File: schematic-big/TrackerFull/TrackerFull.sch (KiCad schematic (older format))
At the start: 60 parts, among them J1 Conn_01x05_Male, J2 MUC-20PFFR-JS7001, J3 Battery, J5 Conn_01x04_Male, J6 78727-0001, Q1 DMG2305UXQ, Q2 DMG2305UXQ, Q3 DMG2305UXQ, SW1 PTS647SK38SMTR2LFS, U1 TLV62585PDRLR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

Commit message: rf
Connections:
- net 2.5v: no longer C9.1, U5.2
- net GPS_POWER: now also C9.1, U5.2
- no-connect marks 38 -> 45
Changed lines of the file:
@@
 Connection ~ 9250 8450
 Wire Wire Line
-	9250 8450 9250 8350
-Wire Wire Line
 	8650 8450 8650 8600
 Wire Wire Line
 	9700 8450 9550 8450
-Text Label 9250 8350 0    50   ~ 0
-2.5v
 $Comp
 L Device:R R6
@@
 Wire Wire Line
 	2950 7500 2950 7750
-Text Label 14650 4950 0    50   ~ 0
-VSIM
 Text GLabel 2950 7650 0    50   Input ~ 0
 BAT_IN
@@
 Text Label 7100 8700 0    50   ~ 0
 ANT_OUT
+NoConn ~ 8150 6350
+NoConn ~ 8150 6450
+NoConn ~ 8150 6550
+NoConn ~ 8150 6650
+NoConn ~ 8150 5850
+NoConn ~ 8150 5550
+NoConn ~ 8150 5450
+Wire Wire Line
+	9150 8450 9250 8450
 $EndSCHEMATC

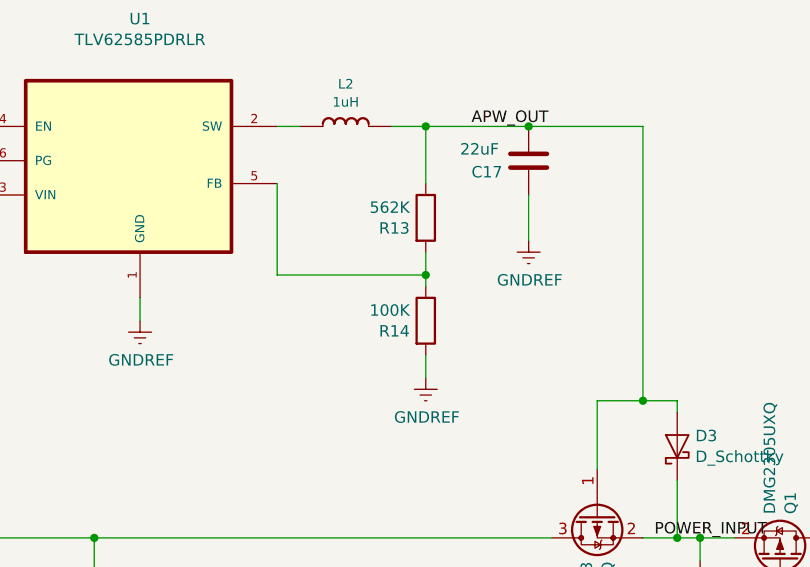
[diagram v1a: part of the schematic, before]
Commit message: attiny461 code update and new a9g footprint
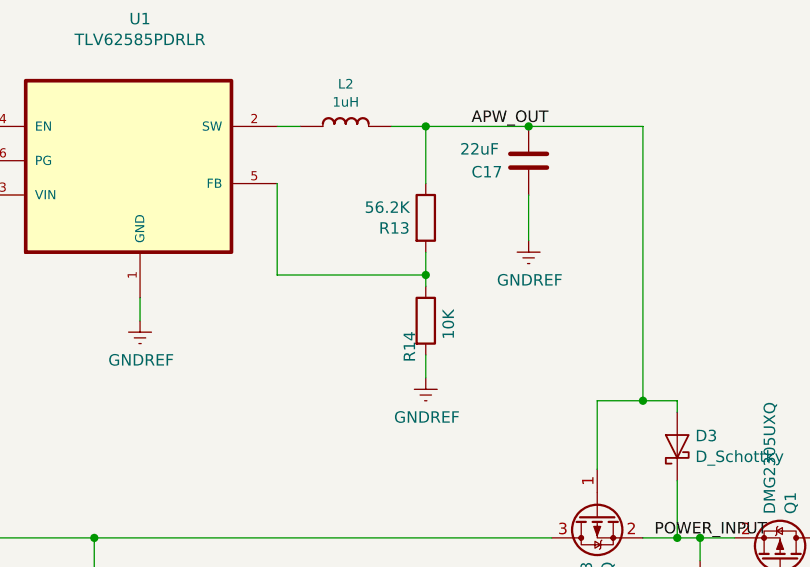
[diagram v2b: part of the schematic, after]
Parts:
- D1: footprint Tracker:A9G2 -> imported:A9
- R13: value 562K -> 56.2K; Поле5 CRCW0603562KFKEBC -> WR06X5622FTL
- R14: value 100K -> 10K; Поле5 CR161003F -> RMCF0603FG10K0
- R17, R5, R6, R7: footprint Resistor_SMD:R_0805_2012Metric_Pad1.15x1.40mm_HandSolder -> Resistor_SMD:R_0603_1608Metric; Поле5 CR0805-8W-103JT -> RMCF0603FG10K0
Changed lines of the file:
@@
 F 0 "R5" V 1830 3704 50  0000 R CNN
 F 1 "10K" V 2000 3800 50  0000 R CNN
-F 2 "Resistor_SMD:R_0805_2012Metric_Pad1.15x1.40mm_HandSolder" H 1830 3841 50  0001 R CNN
-F 3 "https://www.digikey.com/en/products/detail/venkel/CR0805-8W-103JT/12331089" H 1900 3750 50  0001 C CNN
-F 4 "CR0805-8W-103JT" H 1900 3750 50  0001 C CNN "Поле5"
+F 2 "Resistor_SMD:R_0603_1608Metric" H 1830 3841 50  0001 R CNN
+F 3 "https://www.digikey.com/en/products/detail/stackpole-electronics-inc/RMCF0603FG10K0/1761236" H 1900 3750 50  0001 C CNN
+F 4 "RMCF0603FG10K0" H 1900 3750 50  0001 C CNN "Поле5"
 	1    1900 3750
 	1    0    0    -1
@@
 F 0 "R17" V 3250 6350 50  0000 R CNN
 F 1 "10K" V 3200 6200 50  0000 R CNN
-F 2 "Resistor_SMD:R_0805_2012Metric_Pad1.15x1.40mm_HandSolder" H 3130 6241 50  0001 R CNN
-F 3 "https://www.digikey.com/en/products/detail/venkel/CR0805-8W-103JT/12331089" H 3200 6150 50  0001 C CNN
-F 4 "CR0805-8W-103JT" H 3200 6150 50  0001 C CNN "Поле5"
+F 2 "Resistor_SMD:R_0603_1608Metric" H 3130 6241 50  0001 R CNN
+F 3 "https://www.digikey.com/en/products/detail/stackpole-electronics-inc/RMCF0603FG10K0/1761236" H 3200 6150 50  0001 C CNN
+F 4 "RMCF0603FG10K0" H 3200 6150 50  0001 C CNN "Поле5"
 	1    3200 6150
 	0    -1   -1   0
@@
 F 0 "R7" V 3230 6504 50  0000 R CNN
 F 1 "10K" V 3150 6800 50  0000 R CNN
-F 2 "Resistor_SMD:R_0805_2012Metric_Pad1.15x1.40mm_HandSolder" H 3230 6641 50  0001 R CNN
-F 3 "https://www.digikey.com/en/products/detail/venkel/CR0805-8W-103JT/12331089" H 3300 6550 50  0001 C CNN
-F 4 "CR0805-8W-103JT" H 3300 6550 50  0001 C CNN "Поле5"
+F 2 "Resistor_SMD:R_0603_1608Metric" H 3230 6641 50  0001 R CNN
+F 3 "https://www.digikey.com/en/products/detail/stackpole-electronics-inc/RMCF0603FG10K0/1761236" H 3300 6550 50  0001 C CNN
+F 4 "RMCF0603FG10K0" H 3300 6550 50  0001 C CNN "Поле5"
 	1    3300 6550
 	0    -1   -1   0
@@
 F 0 "D1" H 4500 6106 50  0000 C CNN
 F 1 "A9G" H 4500 6015 50  0000 C CNN
-F 2 "Tracker:A9G2" V 3950 4450 50  0001 C CNN
+F 2 "imported:A9" V 3950 4450 50  0001 C CNN
 F 3 "https://www.alibaba.com/product-detail/GPRS-GPS-Module-A9G-Module-SMS_62458730712.html?spm=a2700.galleryofferlist.normal_offer.3.6881306fMlvXSR" V 3950 4450 50  0001 C CNN
 F 4 "3" H 4450 5500 50  0001 C CNN "Поле4"
@@
 F 0 "R6" V 8730 8404 50  0000 R CNN
 F 1 "10K" V 8900 8500 50  0000 R CNN
-F 2 "Resistor_SMD:R_0805_2012Metric_Pad1.15x1.40mm_HandSolder" H 8730 8541 50  0001 R CNN
-F 3 "https://www.digikey.com/en/products/detail/venkel/CR0805-8W-103JT/12331089" H 8800 8450 50  0001 C CNN
-F 4 "CR0805-8W-103JT" H 8800 8450 50  0001 C CNN "Поле5"
+F 2 "Resistor_SMD:R_0603_1608Metric" H 8730 8541 50  0001 R CNN
+F 3 "https://www.digikey.com/en/products/detail/stackpole-electronics-inc/RMCF0603FG10K0/1761236" H 8800 8450 50  0001 C CNN
+F 4 "RMCF0603FG10K0" H 8800 8450 50  0001 C CNN "Поле5"
 	1    8800 8450
 	0    -1   -1   0
@@
 P 8800 1450
 F 0 "R13" H 8730 1404 50  0000 R CNN
-F 1 "562K" H 8730 1495 50  0000 R CNN
+F 1 "56.2K" H 8730 1495 50  0000 R CNN
 F 2 "Resistor_SMD:R_0603_1608Metric" H 8730 1541 50  0001 R CNN
-F 3 "https://www.digikey.com/en/products/detail/vishay-dale/CRCW0603562KFKEBC/7925213" H 8800 1450 50  0001 C CNN
-F 4 "CRCW0603562KFKEBC" H 8800 1450 50  0001 C CNN "Поле5"
+F 3 "https://www.digikey.com/en/products/detail/walsin-technology-corporation/WR06X5622FTL/13241739" H 8800 1450 50  0001 C CNN
+F 4 "WR06X5622FTL" H 8800 1450 50  0001 C CNN "Поле5"
 	1    8800 1450
-	1    0    0    -1
-$EndComp
-$Comp
-L Device:R R14
-U 1 1 5FB5F89D
-P 8800 1900
-F 0 "R14" H 8730 1854 50  0000 R CNN
-F 1 "100K" H 8730 1945 50  0000 R CNN
-F 2 "Resistor_SMD:R_0603_1608Metric" H 8730 1991 50  0001 R CNN
-F 3 "https://www.digikey.com/en/products/detail/meritek/CR161003F/13412806" H 8800 1900 50  0001 C CNN
-F 4 "CR161003F" H 8800 1900 50  0001 C CNN "Поле5"
-	1    8800 1900
 	1    0    0    -1
 $EndComp
@@
 Wire Wire Line
 	9150 8450 9250 8450
+$Comp
+L Device:R R14
+U 1 1 5FB75EE7
+P 8800 1900
+F 0 "R14" V 8730 1854 50  0000 R CNN
+F 1 "10K" V 8900 1950 50  0000 R CNN
+F 2 "Resistor_SMD:R_0603_1608Metric" H 8730 1991 50  0001 R CNN
+F 3 "https://www.digikey.com/en/products/detail/stackpole-electronics-inc/RMCF0603FG10K0/1761236" H 8800 1900 50  0001 C CNN
+F 4 "RMCF0603FG10K0" H 8800 1900 50  0001 C CNN "Поле5"
+	1    8800 1900
+	1    0    0    -1
+$EndComp
 $EndSCHEMATC

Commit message: last changes
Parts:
- added C5: 100nF, Capacitor_SMD:C_0402_1005Metric, symbol Device:C
- added L1: 10uH, Inductor_SMD:L_0603_1608Metric, symbol Device:L
- added Q4: DMN60H080DS, Package_TO_SOT_SMD:SOT-23, symbol Device:Q_NMOS_GSD
- added R16, R20: 10K, Resistor_SMD:R_0603_1608Metric, symbol Device:R
- added R18: 470, Resistor_SMD:R_0402_1005Metric, symbol Device:R
- added R19: 5K, Resistor_SMD:R_0402_1005Metric, symbol Device:R
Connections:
- net 2.5v: now also U8.22 (AREF/PA3)
- net AVR_RST: now also R16.1
- net GNDD: now also C5.2, Q4.2 (S)
- net LOW_CURRENT: now also L1.1, R16.2, R19.1; no longer U8.18 (AVCC)
- net at U8.7 (XTAL1/PB4): now also R18.2
- net ADC_IN: now reaches U8.8 (XTAL2/PB5)
- net ADC_IN: now also R19.2, R20.2
- new net: Q4.3 (D), R20.1
- new net ADC_ENABLE: Q4.1 (G), R18.1
- new net AVCC: C5.1, L1.2, U8.18 (AVCC)
- no-connect marks 45 -> 42

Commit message: last changes
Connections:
- net ACCEL_INT1: now also U8.10 (PB6); no longer U8.25 (PA1)
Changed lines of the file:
@@
 Wire Wire Line
 	8800 1050 9250 1050
-Text Label 8300 5250 0    50   ~ 0
+Text Label 8300 6650 0    50   ~ 0
 ACCEL_INT1
 Wire Wire Line
@@
 	8150 5350 8300 5350
 Wire Wire Line
-	8150 5250 8300 5250
+	8150 6650 8300 6650
 Connection ~ 7450 4450
 Wire Wire Line
@@
 ANT_OUT
 NoConn ~ 8150 6350
-NoConn ~ 8150 6650
 NoConn ~ 8150 5850
 NoConn ~ 8150 5550
@@
 	1    0    0    -1
 $EndComp
+NoConn ~ 8150 5250
+Wire Notes Line
+	4050 450  4050 4350
+Wire Notes Line
+	4050 4350 450  4350
 $EndSCHEMATC

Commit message: last changes
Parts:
- removed SW1: PTS647SK38SMTR2LFS, PTS647SK38SMTR2LFS, symbol PTS647SK38SMTR2LFS:PTS647SK38SMTR2LFS
- R15: value 100K -> 10K; Поле5 CR161003F -> RMCF0603FG10K0
- U7: value MIC5232-2.8YD5 -> LDO-3v3; Поле5 MIC5232-2.8YD5 -> MIC5232-3.3YD5-TR
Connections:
- net 2.5v: now also C13.2, C18.2, L1.1, R16.2, U8.4 (VCC); no longer U8.22 (AREF/PA3)
- net GNDD: no longer J6.7 (DETECT_SPRING)
- net GNDREF: now also R15.2
- net LOW_CURRENT: now also J6.7 (DETECT_SPRING); no longer C13.2, C18.2, L1.1, R16.2, U8.4 (VCC)
- net POWER_INPUT: no longer R15.1
- net SIM_DETECT_LINE: now also R15.1; no longer R15.2
- no-connect marks 42 -> 43
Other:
- moved on the sheet: R16, R18, R3
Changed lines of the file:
@@
 BAT_IN
 NoConn ~ 4000 7500
-Connection ~ 8600 7350
-Wire Wire Line
-	8600 7350 8600 7450
-Wire Wire Line
-	9800 7350 9800 7450
-Connection ~ 9800 7450
-Wire Wire Line
-	9800 7450 9800 7600
 Wire Wire Line
 	3200 2050 3750 2050
@@
 Wire Wire Line
 	8800 1050 9250 1050
-Text Label 8300 6650 0    50   ~ 0
+Text Label 8400 6650 0    50   ~ 0
 ACCEL_INT1
 Wire Wire Line
@@
 Text Label 8600 6250 0    50   ~ 0
 ISP_SCK
-Wire Wire Line
-	8150 6750 8600 6750
 Text Label 8300 5150 0    50   ~ 0
 AVR_MOSI_SDA
@@
 	8150 5350 8300 5350
 Wire Wire Line
-	8150 6650 8300 6650
+	8150 6650 8400 6650
 Connection ~ 7450 4450
 Wire Wire Line
@@
 	7550 7050 7450 7050
 Connection ~ 7450 7050
-Text Label 9550 5650 0    50   ~ 0
+Text Label 9050 5650 0    50   ~ 0
 LED_CTL
 Text Label 9050 5750 0    50   ~ 0
@@
 	8900 5750 9050 5750
 Wire Wire Line
-	8150 5650 8800 5650
-Wire Wire Line
-	9100 5650 9550 5650
+	8150 5650 8600 5650
+Wire Wire Line
+	8900 5650 9050 5650
 Wire Wire Line
 	8150 5750 8600 5750
@@
 Wire Wire Line
 	650  1250 1350 1250
-Text Label 7450 4800 1    50   ~ 0
-LOW_CURRENT
 Text Label 11000 6000 0    50   ~ 0
 LOW_CURRENT
@@
 	1    0    0    -1
 $EndComp
-$Comp
-L power:GNDD #PWR0124
-U 1 1 602328E5
-P 9800 7600
-F 0 "#PWR0124" H 9800 7350 50  0001 C CNN
-F 1 "GNDD" H 9804 7445 50  0000 C CNN
-F 2 "" H 9800 7600 50  0001 C CNN
-F 3 "" H 9800 7600 50  0001 C CNN
-	1    9800 7600
-	1    0    0    -1
-$EndComp
 Wire Wire Line
 	2950 7300 2950 7500
@@
 Text Label 10350 3400 0    50   ~ 0
 SIM_DETECT_LINE
-Wire Wire Line
-	9900 2850 10000 2850
 Connection ~ 9900 2850
 Wire Wire Line
 	10550 2850 11350 2850
-Wire Wire Line
-	10000 2850 10000 2950
-Connection ~ 10000 2850
-Wire Wire Line
-	10000 2850 10150 2850
 Wire Wire Line
 	10000 3250 10350 3250
@@
 	10350 3400 10350 3250
 Connection ~ 10350 3250
-$Comp
-L power:GNDD #PWR0115
-U 1 1 5FB652B8
-P 2500 9050
-F 0 "#PWR0115" H 2500 8800 50  0001 C CNN
-F 1 "GNDD" H 2504 8895 50  0000 C CNN
-F 2 "" H 2500 9050 50  0001 C CNN
-F 3 "" H 2500 9050 50  0001 C CNN
-	1    2500 9050
-	1    0    0    -1
-$EndComp
 Wire Wire Line
 	1850 9050 2500 9050
-Text Label 2300 8450 0    50   ~ 0
+Text Label 2500 8450 0    50   ~ 0
 SIM_DETECT_LINE
 Wire Wire Line
@@
 Wire Wire Line
 	9150 8450 9250 8450
-Text Label 9700 6300 2    50   ~ 0
-LOW_CURRENT
-Wire Wire Line
-	9700 6750 9700 6700
-Wire Wire Line
-	9700 6300 9700 6400
+Wire Wire Line
+	9400 6750 9300 6750
 $Comp
 L power:GNDD #PWR0129
@@
 	7450 4050 7450 3950
 Connection ~ 7450 4050
-Wire Wire Line
-	8600 6750 8600 7350
 Text Label 8600 6750 0    50   ~ 0
 AVR_RST
-Wire Wire Line
-	8600 6750 9700 6750
-Connection ~ 8600 6750
 $Comp
 L power:GNDD #PWR0130
@@
 Wire Wire Line
 	11600 8350 12000 8350
-Text Label 8300 5450 0    50   ~ 0
-2.5v
-Wire Wire Line
-	8150 5450 8300 5450
-Text Label 9000 6450 0    50   ~ 0
+Text Label 9100 6450 0    50   ~ 0
 ADC_ENABLE
 Wire Wire Line
-	8750 6450 9000 6450
-Wire Wire Line
-	8150 6450 8450 6450
+	8900 6450 9100 6450
+Wire Wire Line
+	8150 6450 8600 6450
 Wire Wire Line
 	4850 550  5000 550
@@
 L Device:R R18
 U 1 1 5FBD9E28
-P 8600 6450
-F 0 "R18" V 8530 6404 50  0000 R CNN
-F 1 "470" V 8550 6750 50  0000 R CNN
-F 2 "Resistor_SMD:R_0402_1005Metric" H 8530 6541 50  0001 R CNN
-F 3 "https://www.digikey.com/en/products/detail/venkel/CR0402-16W-4700FT/12332416" H 8600 6450 50  0001 C CNN
-F 4 "CR0402-16W-4700FT" H 8600 6450 50  0001 C CNN "Поле5"
-	1    8600 6450
+P 8750 6450
+F 0 "R18" V 8750 6500 50  0000 R CNN
+F 1 "470" V 8700 6300 50  0000 R CNN
+F 2 "Resistor_SMD:R_0402_1005Metric" H 8680 6541 50  0001 R CNN
+F 3 "https://www.digikey.com/en/products/detail/venkel/CR0402-16W-4700FT/12332416" H 8750 6450 50  0001 C CNN
+F 4 "CR0402-16W-4700FT" H 8750 6450 50  0001 C CNN "Поле5"
+	1    8750 6450
 	0    1    1    0
 $EndComp
@@
 L Device:R R16
 U 1 1 5FCEF734
-P 9700 6550
-F 0 "R16" V 9630 6504 50  0000 R CNN
-F 1 "10K" V 9800 6600 50  0000 R CNN
-F 2 "Resistor_SMD:R_0603_1608Metric" H 9630 6641 50  0001 R CNN
-F 3 "https://www.digikey.com/en/products/detail/stackpole-electronics-inc/RMCF0603FG10K0/1761236" H 9700 6550 50  0001 C CNN
-F 4 "RMCF0603FG10K0" H 9700 6550 50  0001 C CNN "Поле5"
-	1    9700 6550
-	-1   0    0    1
+P 9150 6750
+F 0 "R16" V 9080 6704 50  0000 R CNN
+F 1 "10K" V 9250 6800 50  0000 R CNN
+F 2 "Resistor_SMD:R_0603_1608Metric" H 9080 6841 50  0001 R CNN
+F 3 "https://www.digikey.com/en/products/detail/stackpole-electronics-inc/RMCF0603FG10K0/1761236" H 9150 6750 50  0001 C CNN
+F 4 "RMCF0603FG10K0" H 9150 6750 50  0001 C CNN "Поле5"
+	1    9150 6750
+	0    -1   -1   0
 $EndComp
 $Comp
@@
 F 4 "78727-0001" H 1950 7850 50  0001 C CNN "Поле5"
 	1    1950 7850
-	1    0    0    -1
-$EndComp
-$Comp
-L Device:R R15
-U 1 1 5FB9E73A
-P 10000 3100
-F 0 "R15" H 9950 3100 50  0000 L CNN
-F 1 "100K" H 9850 3000 50  0000 L CNN
-F 2 "Resistor_SMD:R_0603_1608Metric" H 10070 3009 50  0001 L CNN
-F 3 "https://www.digikey.com/en/products/detail/meritek/CR161003F/13412806" H 10000 3100 50  0001 C CNN
-F 4 "CR161003F" H 10000 3100 50  0001 C CNN "Поле5"
-	1    10000 3100
 	1    0    0    -1
 $EndComp
@@
 U 1 1 5FAA6E90
 P 8750 5750
-F 0 "R2" V 8680 5704 50  0000 R CNN
-F 1 "470" V 8850 5800 50  0000 R CNN
+F 0 "R2" V 8750 5800 50  0000 R CNN
+F 1 "470" V 8700 5600 50  0000 R CNN
 F 2 "Resistor_SMD:R_0402_1005Metric" H 8680 5841 50  0001 R CNN
 F 3 "https://www.digikey.com/en/products/detail/venkel/CR0402-16W-4700FT/12332416" H 8750 5750 50  0001 C CNN
@@
 L Device:R R3
 U 1 1 5FAA6E85
-P 8950 5650
-F 0 "R3" V 8950 5700 50  0000 R CNN
-F 1 "470" V 9000 5950 50  0000 R CNN
-F 2 "Resistor_SMD:R_0402_1005Metric" H 8880 5741 50  0001 R CNN
-F 3 "https://www.digikey.com/en/products/detail/venkel/CR0402-16W-4700FT/12332416" H 8950 5650 50  0001 C CNN
-F 4 "CR0402-16W-4700FT" H 8950 5650 50  0001 C CNN "Поле5"
-	1    8950 5650
+P 8750 5650
+F 0 "R3" V 8750 5700 50  0000 R CNN
+F 1 "470" V 8800 5950 50  0000 R CNN
+F 2 "Resistor_SMD:R_0402_1005Metric" H 8680 5741 50  0001 R CNN
+F 3 "https://www.digikey.com/en/products/detail/venkel/CR0402-16W-4700FT/12332416" H 8750 5650 50  0001 C CNN
+F 4 "CR0402-16W-4700FT" H 8750 5650 50  0001 C CNN "Поле5"
+	1    8750 5650
 	0    -1   -1   0
 $EndComp
@@
 $EndComp
 $Comp
-L PTS647SK38SMTR2LFS:PTS647SK38SMTR2LFS SW1
-U 1 1 5F9A40F7
-P 8600 7350
-F 0 "SW1" H 9200 7617 50  0000 C CNN
-F 1 "PTS647SK38SMTR2LFS" H 9200 7526 50  0000 C CNN
-F 2 "PTS647SK38SMTR2LFS" H 8600 7350 50  0001 L BNN
-F 3 "https://www.digikey.com/en/products/detail/c-k/PTS-647-SK38-SMTR2-LFS/9649862" H 8600 7350 50  0001 L BNN
-F 4 "" H 8600 7350 50  0001 L BNN "Поле4"
-F 5 "611-PTS647SK38SMTR2L" H 8600 7350 50  0001 L BNN "Поле5"
-F 6 "3.8mm" H 8600 7350 50  0001 L BNN "Поле6"
-F 7 "Tactile Switches 50mA 12VDC, 2.5N 3.8mm H, G leads" H 8600 7350 50  0001 L BNN "Поле7"
-F 8 "C & K COMPONENTS" H 8600 7350 50  0001 L BNN "Поле8"
-	1    8600 7350
-	1    0    0    -1
-$EndComp
-$Comp
 L Device:R R5
 U 1 1 5F919A02
@@
 P 1950 1350
 F 0 "U7" H 1950 1717 50  0000 C CNN
-F 1 "MIC5232-2.8YD5" H 1950 1626 50  0000 C CNN
+F 1 "LDO-3v3" H 1950 1626 50  0000 C CNN
 F 2 "Package_TO_SOT_SMD:SOT-23-5" H 1950 950 50  0001 C CNN
 F 3 "https://ru.mouser.com/datasheet/2/268/mic5232-1082293.pdf" H 1700 1600 50  0001 C CNN
-F 4 "MIC5232-2.8YD5" H 1950 1350 50  0001 C CNN "Поле5"
+F 4 "MIC5232-3.3YD5-TR" H 1950 1350 50  0001 C CNN "Поле5"
 	1    1950 1350
 	1    0    0    -1
@@
 Wire Notes Line
 	4050 4350 450  4350
+Wire Wire Line
+	9900 2850 10150 2850
+Wire Wire Line
+	10000 3550 10000 3650
+$Comp
+L Device:R R15
+U 1 1 5FD99851
+P 10000 3400
+F 0 "R15" V 9900 3450 50  0000 R CNN
+F 1 "10K" V 10100 3450 50  0000 R CNN
+F 2 "Resistor_SMD:R_0603_1608Metric" H 9930 3491 50  0001 R CNN
+F 3 "https://www.digikey.com/en/products/detail/stackpole-electronics-inc/RMCF0603FG10K0/1761236" H 10000 3400 50  0001 C CNN
+F 4 "RMCF0603FG10K0" H 10000 3400 50  0001 C CNN "Поле5"
+	1    10000 3400
+	1    0    0    -1
+$EndComp
+Text Label 2500 9050 0    50   ~ 0
+LOW_CURRENT
+$Comp
+L power:GNDREF #PWR0115
+U 1 1 5FDFE28A
+P 10000 3650
+F 0 "#PWR0115" H 10000 3400 50  0001 C CNN
+F 1 "GNDREF" H 10000 3500 50  0000 C CNN
+F 2 "" H 10000 3650 50  0001 C CNN
+F 3 "" H 10000 3650 50  0001 C CNN
+	1    10000 3650
+	1    0    0    -1
+$EndComp
+Text Label 7450 3950 0    50   ~ 0
+2.5v
+NoConn ~ 8150 5450
+Text Label 9400 6750 0    50   ~ 0
+2.5v
+Wire Wire Line
+	8150 6750 9000 6750
 $EndSCHEMATC

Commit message: pcb update
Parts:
- removed J2: MUC-20PFFR-JS7001, AMPHENOL_MUC-20PFFR-JS7001, symbol MUC-20PFFR-JS7001:MUC-20PFFR-JS7001
- added J2: USB, Connector_Wire:SolderWirePad_1x02_P3.81mm_Drill0.8mm, symbol Connector:Screw_Terminal_01x02
- J3: footprint Connector_JST:JST_PH_B2B-PH-K_1x02_P2.00mm_Vertical -> Connector_Wire:SolderWirePad_1x02_P3.81mm_Drill0.8mm; Поле5 B2B-PH-K-S(LF)(SN) -> (none)
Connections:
- net +5V: now also J2.1 (Pin_1)
- net CHARGER_STAT: now also D1.19 (LCD_CS/IO15); no longer D1.8 (SD_CLK/IO8)
- net GNDREF: now also J2.2 (Pin_2)
- net at D1.20 (LCD_RST/IO14): now also R17.2
- net at D1.5 (SD_D1/IO11): no longer R17.2
- no-connect marks 43 -> 39
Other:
- moved on the sheet: R17
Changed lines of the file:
@@
 NoConn ~ 4100 7500
 Wire Wire Line
-	3050 6150 2850 6150
-Text Label 2850 6150 0    50   ~ 0
+	4300 7900 4300 8100
+Text Label 4300 8100 3    50   ~ 0
 +5V
 NoConn ~ 3450 5950
@@
 NoConn ~ 3450 6350
 Wire Wire Line
-	3450 6450 2950 6450
-Text Label 2950 6450 0    50   ~ 0
+	4200 7500 4200 8000
+Text Label 4200 8000 3    50   ~ 0
 CHARGER_STAT
 $Comp
@@
 Connection ~ 2400 7100
 Wire Wire Line
-	3350 6150 3450 6150
+	4300 7600 4300 7500
 Text Label 5800 6850 2    50   ~ 0
 GPS_POWER
@@
 Wire Wire Line
 	10150 9100 10250 9100
-NoConn ~ 4850 750
-NoConn ~ 4850 950
-NoConn ~ 4850 850
 Text Label 5050 1050 2    50   ~ 0
 +5V
@@
 Connection ~ 5100 9350
 Connection ~ 5500 9350
-NoConn ~ 4200 7500
 Wire Wire Line
 	750  3100 750  3500
@@
 Text Label 1700 3200 2    50   ~ 0
 AVR_MOSI_SDA
-NoConn ~ 4300 7500
 NoConn ~ 4400 7500
 NoConn ~ 4500 7500
@@
 Wire Wire Line
 	8150 6450 8600 6450
-Wire Wire Line
-	4850 550  5000 550
-NoConn ~ 5000 550
 $Comp
 L Device:R R18
@@
 $EndComp
 $Comp
-L MUC-20PFFR-JS7001:MUC-20PFFR-JS7001 J2
-U 1 1 5FA008B3
-P 4650 850
-F 0 "J2" H 4978 872 50  0000 L CNN
-F 1 "MUC-20PFFR-JS7001" H 4978 781 50  0000 L CNN
-F 2 "AMPHENOL_MUC-20PFFR-JS7001" H 4650 850 50  0001 L BNN
-F 3 "https://www.amphenolltw.com/p2-products-detail.php?sn=4282" H 4650 850 50  0001 L BNN
-F 4 "MUC-20PFFR-JS7001" H 4650 850 50  0001 C CNN "Поле5"
-	1    4650 850
-	-1   0    0    1
-$EndComp
-$Comp
 L Filter:SF14-1575F5UUC1 FL1
 U 1 1 5F9AA44C
@@
 F 0 "J3" V 7350 3650 50  0000 R CNN
 F 1 "Battery" V 7450 3750 50  0000 R CNN
-F 2 "Connector_JST:JST_PH_B2B-PH-K_1x02_P2.00mm_Vertical" H 7350 3500 50  0001 C CNN
-F 3 "https://www.digikey.com/en/products/detail/jst-sales-america-inc/B2B-PH-K-S-LF-SN/926611" H 7350 3500 50  0001 C CNN
-F 4 "B2B-PH-K-S(LF)(SN)" H 7350 3500 50  0001 C CNN "Поле5"
+F 2 "Connector_Wire:SolderWirePad_1x02_P3.81mm_Drill0.8mm" H 7350 3500 50  0001 C CNN
+F 3 "" H 7350 3500 50  0001 C CNN
+F 4 "" H 7350 3500 50  0001 C CNN "Поле5"
 	1    7350 3500
 	0    1    1    0
@@
 L Device:R R17
 U 1 1 5F85A184
-P 3200 6150
-F 0 "R17" V 3300 6200 50  0000 R CNN
-F 1 "10K" V 3200 6200 50  0000 R CNN
-F 2 "Resistor_SMD:R_0603_1608Metric" H 3130 6241 50  0001 R CNN
-F 3 "https://www.digikey.com/en/products/detail/stackpole-electronics-inc/RMCF0603FG10K0/1761236" H 3200 6150 50  0001 C CNN
-F 4 "RMCF0603FG10K0" H 3200 6150 50  0001 C CNN "Поле5"
-	1    3200 6150
-	0    -1   -1   0
+P 4300 7750
+F 0 "R17" V 4400 7800 50  0000 R CNN
+F 1 "10K" V 4300 7800 50  0000 R CNN
+F 2 "Resistor_SMD:R_0603_1608Metric" H 4230 7841 50  0001 R CNN
+F 3 "https://www.digikey.com/en/products/detail/stackpole-electronics-inc/RMCF0603FG10K0/1761236" H 4300 7750 50  0001 C CNN
+F 4 "RMCF0603FG10K0" H 4300 7750 50  0001 C CNN "Поле5"
+	1    4300 7750
+	-1   0    0    1
 $EndComp
 $Comp
@@
 $EndComp
 NoConn ~ 8150 5250
-Wire Notes Line
-	4050 450  4050 4350
-Wire Notes Line
-	4050 4350 450  4350
 Wire Wire Line
 	9900 2850 10150 2850
@@
 Wire Wire Line
 	8150 6750 9000 6750
+$Comp
+L Connector:Screw_Terminal_01x02 J2
+U 1 1 5FD7857D
+P 4650 1050
+F 0 "J2" V 4650 1200 50  0000 R CNN
+F 1 "USB" V 4750 1300 50  0000 R CNN
+F 2 "Connector_Wire:SolderWirePad_1x02_P3.81mm_Drill0.8mm" H 4650 1050 50  0001 C CNN
+F 3 "" H 4650 1050 50  0001 C CNN
+F 4 "" H 4650 1050 50  0001 C CNN "Поле5"
+	1    4650 1050
+	-1   0    0    1
+$EndComp
+Wire Wire Line
+	4850 950  4850 650
+NoConn ~ 3450 6150
+NoConn ~ 3450 6450
 $EndSCHEMATC
